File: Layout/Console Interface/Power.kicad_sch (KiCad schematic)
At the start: 7 parts, among them Q1 AO3401A, U5 MIC5504-3.3YM5

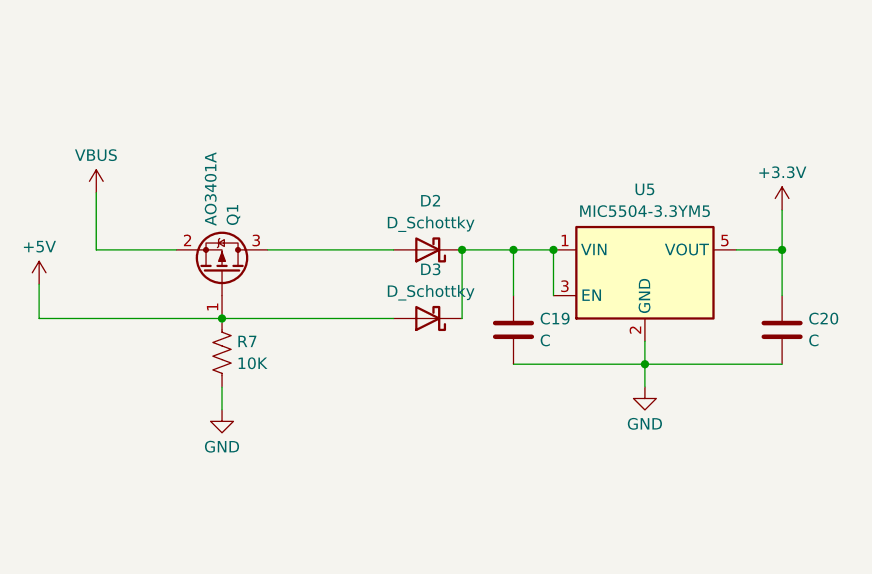
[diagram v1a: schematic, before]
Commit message: Add console interface schematic
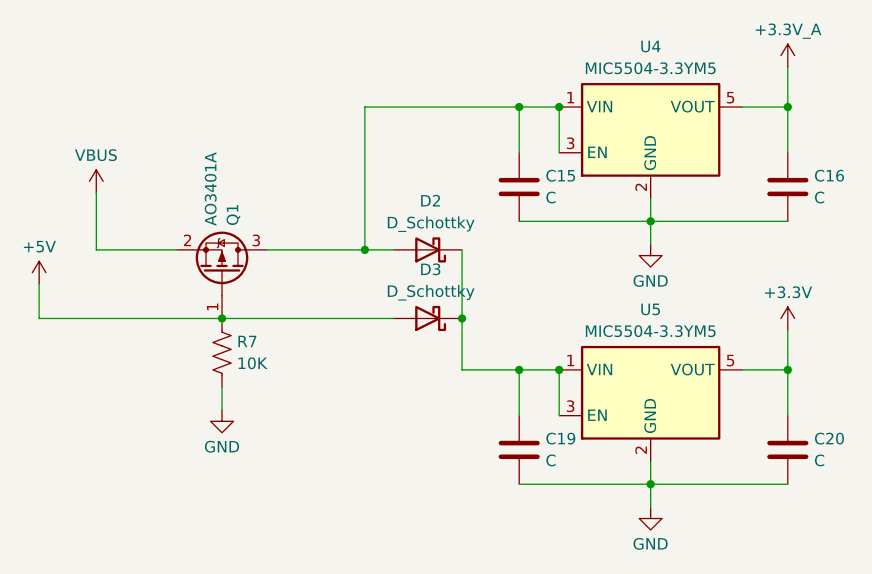
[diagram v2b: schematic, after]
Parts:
- added C15, C16: C, Capacitor_SMD:C_0603_1608Metric, symbol Device:C
- added U4: MIC5504-3.3YM5, Package_TO_SOT_SMD:SOT-23-5, symbol Regulator_Linear:MIC5504-3.3YM5
- C19, C20: footprint Capacitor_SMD:C_0805_2012Metric -> Capacitor_SMD:C_0603_1608Metric
- R7: footprint Resistor_SMD:R_0805_2012Metric -> Resistor_SMD:R_0603_1608Metric
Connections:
- net GND: now also C15.2, C16.2, U4.2 (GND)
- net at D2.2 (A), Q1.3 (D): now also C15.1, U4.1 (VIN), U4.3 (EN)
- new net +3.3V_A: C16.1, U4.5 (VOUT)
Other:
- moved on the sheet: C19, C20, U5

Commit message: Use separate board for lights
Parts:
- D2, D3: footprint Diode_SMD:D_0805_2012Metric -> Diode_SMD:D_0603_1608Metric
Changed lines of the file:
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@@
       (effects (font (size 1.27 1.27)))
     )
-    (property "Footprint" "Diode_SMD:D_0805_2012Metric" (at 139.065 87.63 0)
+    (property "Footprint" "Diode_SMD:D_0603_1608Metric" (at 139.065 87.63 0)
       (effects (font (size 1.27 1.27)) hide)
     )
@@
       (effects (font (size 1.27 1.27)))
     )
-    (property "Footprint" "Diode_SMD:D_0805_2012Metric" (at 139.065 80.01 0)
+    (property "Footprint" "Diode_SMD:D_0603_1608Metric" (at 139.065 80.01 0)
       (effects (font (size 1.27 1.27)) hide)
     )
